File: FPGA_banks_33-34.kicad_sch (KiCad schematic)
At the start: 1 part

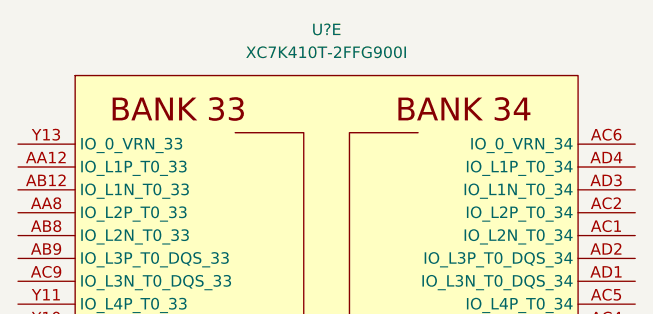
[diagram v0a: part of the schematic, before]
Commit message: Add MT41K512M8DA DDR3L
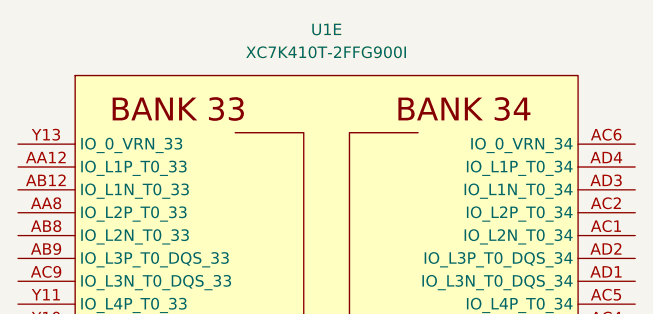
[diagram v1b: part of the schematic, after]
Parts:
- gave numbers to parts that had none: 1
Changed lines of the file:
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@@
   (symbol (lib_id "antmicroMicrocontrollers:XC7K410T-2FFG900I") (at 209.55 130.81 0) (unit 5)
     (in_bom yes) (on_board yes) (fields_autoplaced)
-    (property "Reference" "U?" (id 0) (at 209.55 57.15 0))
+    (property "Reference" "U1" (id 0) (at 209.55 57.15 0))
     (property "Value" "XC7K410T-2FFG900I" (id 1) (at 209.55 59.69 0))
     (property "Footprint" "antmicro-footprints:xc7k410t-2ffg900I" (id 2) (at 209.55 205.74 0)

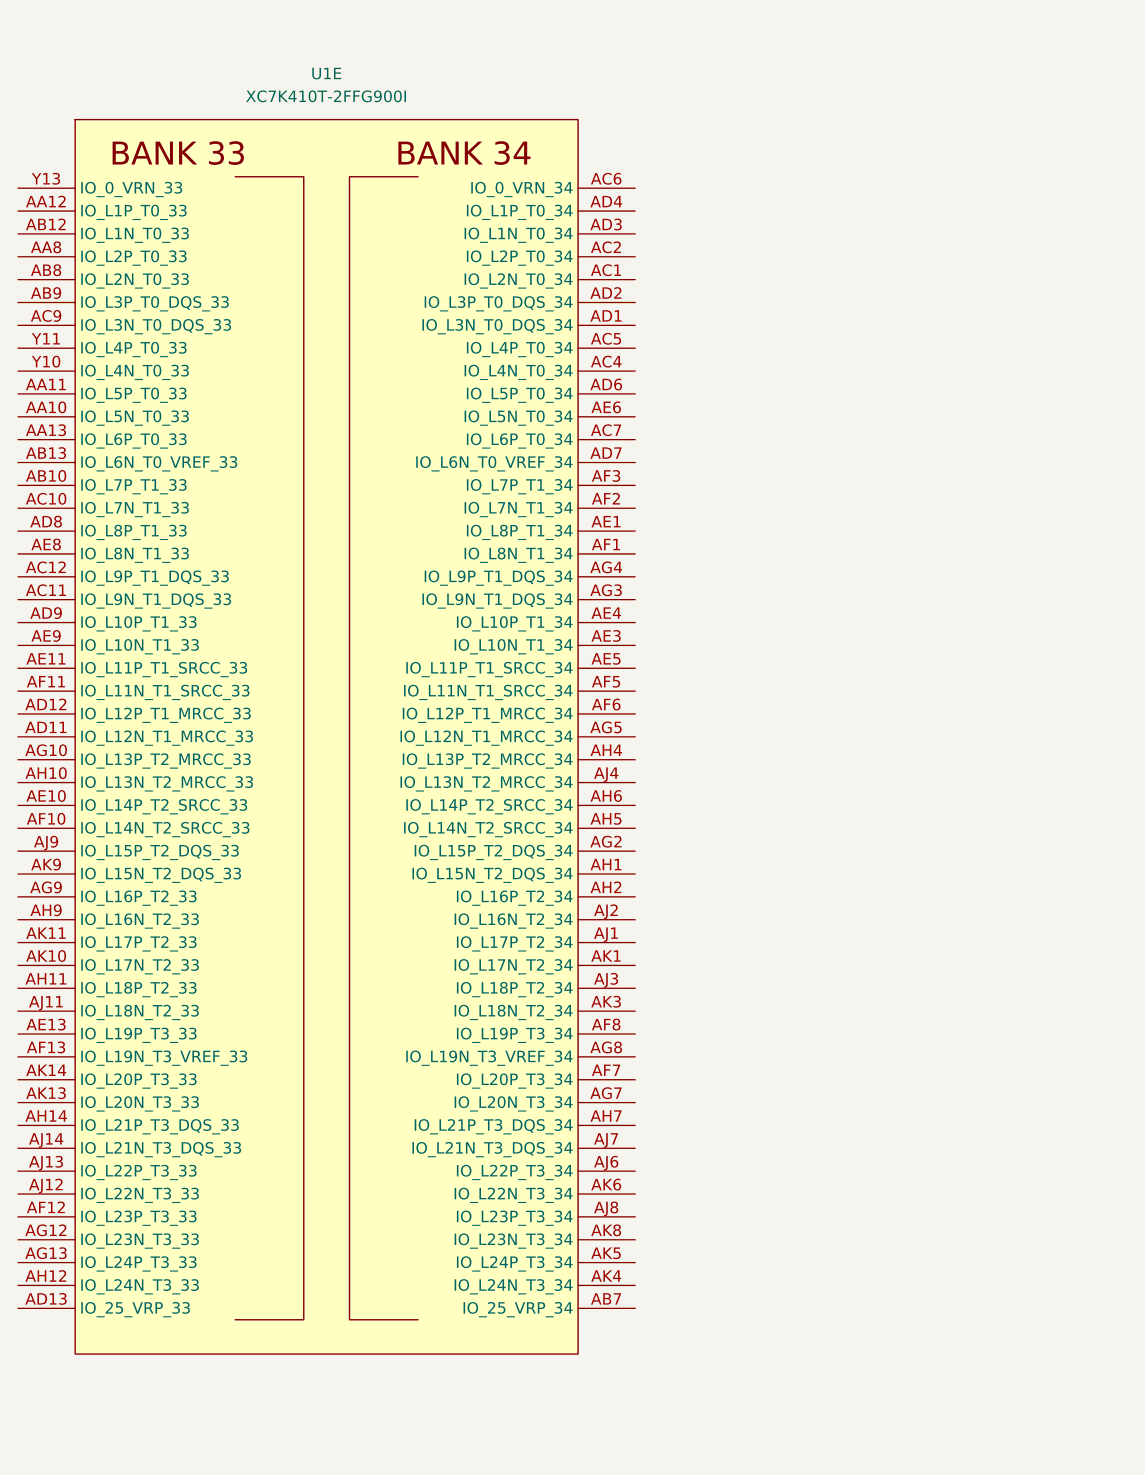
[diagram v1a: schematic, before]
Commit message: Connect DDR3L to FPGA
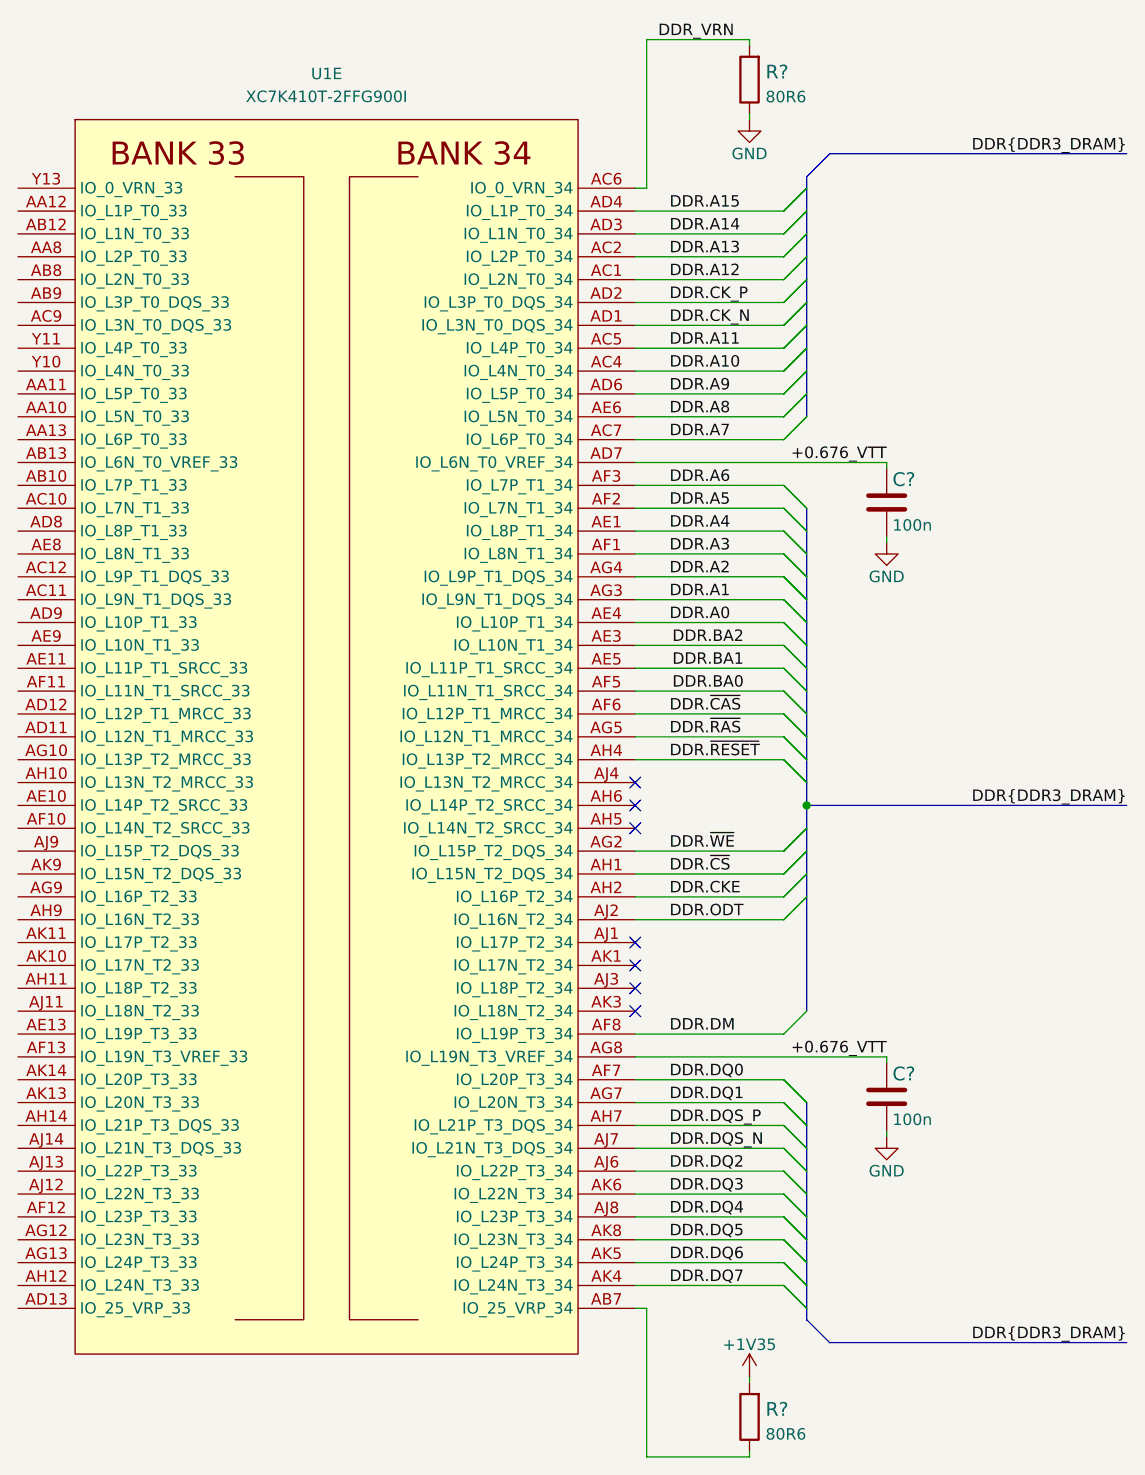
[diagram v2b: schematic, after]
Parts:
- added C? (x2): C_100n_0201, antmicro-footprints:0201-res, symbol antmicroCapacitorsmisc:C_100n_0201
- added R? (x2): R_80R6_0402, antmicro-footprints:0402-res, symbol antmicroResistors0402:R_80R6_0402
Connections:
- net at U1.AB7 (IO_25_VRP_34): now also R?.1
- net DDR.A12: now reaches U1.AC1 (IO_L2N_T0_34)
- net DDR.A13: now reaches U1.AC2 (IO_L2P_T0_34)
- net DDR.A10: now reaches U1.AC4 (IO_L4N_T0_34)
- net DDR.A11: now reaches U1.AC5 (IO_L4P_T0_34)
- net DDR_VRN: now reaches U1.AC6 (IO_0_VRN_34)
- net DDR_VRN: now also R?.2
- net DDR.A7: now reaches U1.AC7 (IO_L6P_T0_34)
- net DDR.CK_N: now reaches U1.AD1 (IO_L3N_T0_DQS_34)
- net DDR.CK_P: now reaches U1.AD2 (IO_L3P_T0_DQS_34)
- net DDR.A14: now reaches U1.AD3 (IO_L1N_T0_34)
- net DDR.A15: now reaches U1.AD4 (IO_L1P_T0_34)
- net DDR.A9: now reaches U1.AD6 (IO_L5P_T0_34)
- net +0.676_VTT: now reaches U1.AD7 (IO_L6N_T0_VREF_34)
- net +0.676_VTT: now also U1.AG8 (IO_L19N_T3_VREF_34), C?.1, C?.1
- net DDR.A4: now reaches U1.AE1 (IO_L8P_T1_34)
- net DDR.BA2: now reaches U1.AE3 (IO_L10N_T1_34)
- net DDR.A0: now reaches U1.AE4 (IO_L10P_T1_34)
- net DDR.BA1: now reaches U1.AE5 (IO_L11P_T1_SRCC_34)
- net DDR.A8: now reaches U1.AE6 (IO_L5N_T0_34)
- net DDR.A3: now reaches U1.AF1 (IO_L8N_T1_34)
- net DDR.A5: now reaches U1.AF2 (IO_L7N_T1_34)
- net DDR.A6: now reaches U1.AF3 (IO_L7P_T1_34)
- net DDR.BA0: now reaches U1.AF5 (IO_L11N_T1_SRCC_34)
- net DDR.~{CAS}: now reaches U1.AF6 (IO_L12P_T1_MRCC_34)
- net DDR.DQ0: now reaches U1.AF7 (IO_L20P_T3_34)
- net DDR.DM: now reaches U1.AF8 (IO_L19P_T3_34)
- net DDR.~{WE}: now reaches U1.AG2 (IO_L15P_T2_DQS_34)
- net DDR.A1: now reaches U1.AG3 (IO_L9N_T1_DQS_34)
- net DDR.A2: now reaches U1.AG4 (IO_L9P_T1_DQS_34)
- net DDR.~{RAS}: now reaches U1.AG5 (IO_L12N_T1_MRCC_34)
- net DDR.DQ1: now reaches U1.AG7 (IO_L20N_T3_34)
- net DDR.~{CS}: now reaches U1.AH1 (IO_L15N_T2_DQS_34)
- net DDR.CKE: now reaches U1.AH2 (IO_L16P_T2_34)
- net DDR.~{RESET}: now reaches U1.AH4 (IO_L13P_T2_MRCC_34)
- net DDR.DQS_P: now reaches U1.AH7 (IO_L21P_T3_DQS_34)
- net DDR.ODT: now reaches U1.AJ2 (IO_L16N_T2_34)
- net DDR.DQ2: now reaches U1.AJ6 (IO_L22P_T3_34)
- net DDR.DQS_N: now reaches U1.AJ7 (IO_L21N_T3_DQS_34)
- net DDR.DQ4: now reaches U1.AJ8 (IO_L23P_T3_34)
- net DDR.DQ7: now reaches U1.AK4 (IO_L24N_T3_34)
- net DDR.DQ6: now reaches U1.AK5 (IO_L24P_T3_34)
- net DDR.DQ3: now reaches U1.AK6 (IO_L22N_T3_34)
- net DDR.DQ5: now reaches U1.AK8 (IO_L23N_T3_34)
- new net +1V35: R?.2
- new net GND: C?.2, C?.2, R?.1
- no-connect marks 0 -> 7

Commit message: Unify title block
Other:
- title: (none) -> K410T devboard
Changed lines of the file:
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@@
   (paper "A3")
   (title_block
-    (comment 1 "www.antmicro.com")
-    (comment 2 "Antmicro Ltd")
+    (title "K410T devboard")
+    (date "2022-12-20")
+    (rev "0.0.99")
   )
   (junction (at 262.89 138.43) (diameter 0) (color 0 0 0 0)
@@
   (symbol (lib_id "power:GND") (at 271.78 109.22 0) (unit 1)
     (in_bom yes) (on_board yes)
-    (property "Reference" "#PWR?" (id 0) (at 271.78 115.57 0)
+    (property "Reference" "#PWR0118" (id 0) (at 271.78 115.57 0)
       (effects (font (size 1.27 1.27)) hide)
     )
@@
   (symbol (lib_id "power:+1V35") (at 256.54 201.93 0) (unit 1)
     (in_bom yes) (on_board yes) (fields_autoplaced)
-    (property "Reference" "#PWR?" (id 0) (at 256.54 205.74 0)
+    (property "Reference" "#PWR0117" (id 0) (at 256.54 205.74 0)
       (effects (font (size 1.27 1.27)) hide)
     )
@@
   (symbol (lib_id "power:GND") (at 271.78 175.26 0) (unit 1)
     (in_bom yes) (on_board yes)
-    (property "Reference" "#PWR?" (id 0) (at 271.78 181.61 0)
+    (property "Reference" "#PWR0120" (id 0) (at 271.78 181.61 0)
       (effects (font (size 1.27 1.27)) hide)
     )
@@
   (symbol (lib_id "power:GND") (at 256.54 62.23 0) (unit 1)
     (in_bom yes) (on_board yes)
-    (property "Reference" "#PWR?" (id 0) (at 256.54 68.58 0)
+    (property "Reference" "#PWR0119" (id 0) (at 256.54 68.58 0)
       (effects (font (size 1.27 1.27)) hide)
     )
